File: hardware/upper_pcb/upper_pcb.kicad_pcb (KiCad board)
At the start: 2 copper layers, 54 x 54 mm, 12 parts, among them J5 FPC-6P-0.5mm, SW4 Kailh-GM8.0, SW5 Kailh-GM8.0, SW6 Kailh-BlueDot, SW7 Kailh-BlueDot

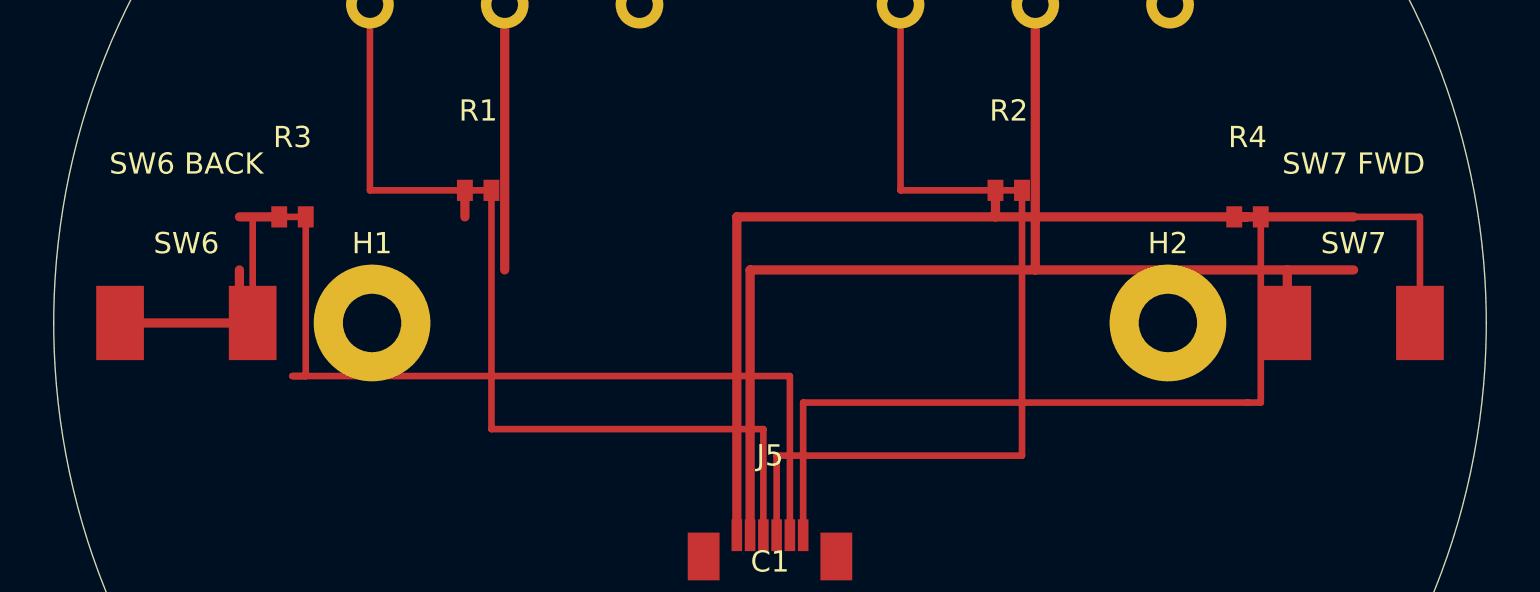
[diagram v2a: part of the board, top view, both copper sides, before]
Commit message: feat: replace SW6/SW7 Blue Dot SMD with Alps SKHLLBA010 side-push THT
- SKHLLBA010: side-push tact switch, 4 THT holes in 6.5x6.5mm square
- 1.57N actuation (firmer = intentional for Back/Fwd nav buttons)
- 50k cycle life, DigiKey stocked ~0.53ea, JLCPCB LCSC C115343
- Footprint: 4x Ø1.0mm holes, 1.8mm pads, signal+GND+2xsnap-in legs
- Updated: gen_kicad_pcb.py, gen_gerbers.py, add_traces.py
- Traces: R3/R4 pull-ups repositioned, signal routes to correct hole coords
- Silkscreen: SKHLLBA010 label, body outline 7.3x7.22mm, pin1 marker
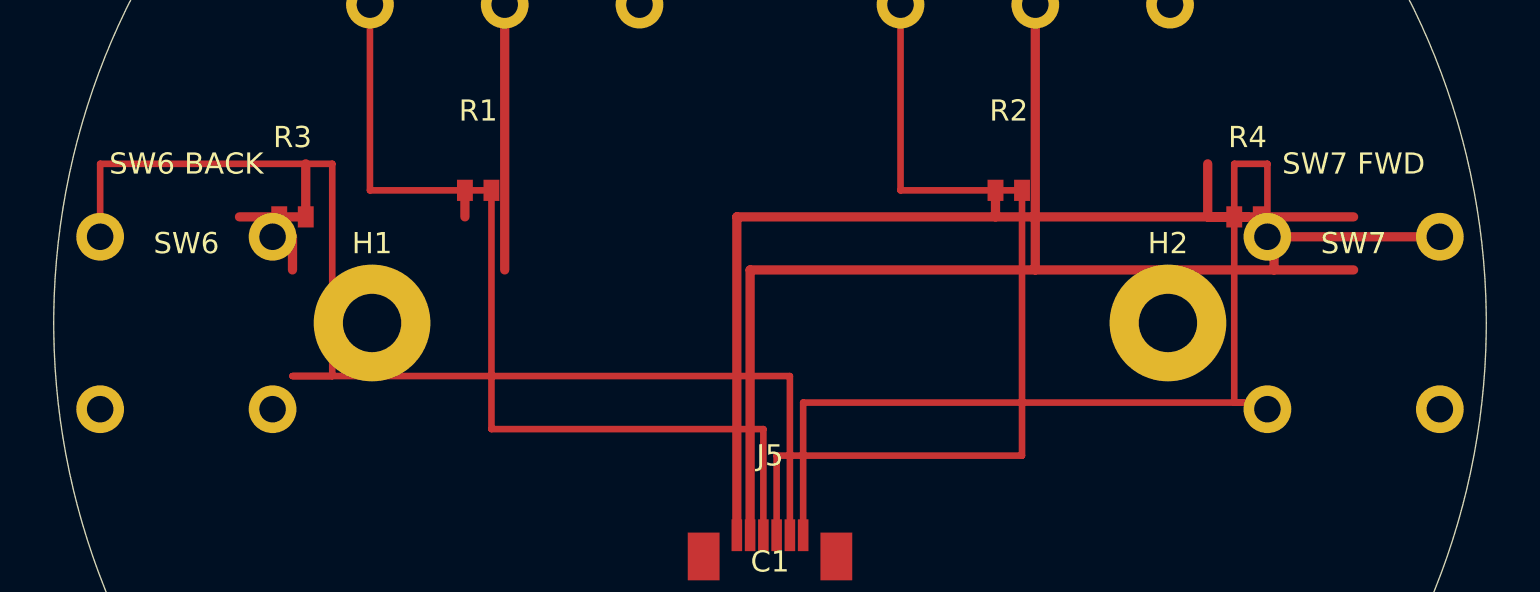
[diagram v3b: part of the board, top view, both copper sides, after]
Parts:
- SW6, SW7: value Kailh-BlueDot -> Alps-SKHLLBA010
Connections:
- SW6 pad 1: GND -> BTN_BK
- SW6 pad 2: BTN_BK -> GND
- SW7 pad 1: GND -> BTN_FW
- SW7 pad 2: BTN_FW -> GND
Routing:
- net BTN_BK: track 37.2 -> 45.8 mm
- net 3V3: track 39.2 -> 45.2 mm
- net BTN_FW: track 39.2 -> 35.2 mm
- net GND: track 61.2 -> 62.2 mm
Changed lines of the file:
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@@
   (footprint "SW6" (layer "F.Cu") (at 78.0000 100.0000 0)
     (fp_text reference "SW6" (at 0 -3) (layer "F.SilkS") (effects (font (size 0.8 0.8) (thickness 0.15))))
-    (fp_text value "Kailh-BlueDot" (at 0 3) (layer "F.Fab") hide)
-    (pad "1" smd rect (at -2.5000 0.0000) (size 1.8000 2.8000)
-      (layers "F.Cu" "F.Mask") (net 1 "GND"))
-    (pad "2" smd rect (at 2.5000 0.0000) (size 1.8000 2.8000)
-      (layers "F.Cu" "F.Mask") (net 5 "BTN_BK"))
+    (fp_text value "Alps-SKHLLBA010" (at 0 3) (layer "F.Fab") hide)
+    (pad "1" thru_hole circle (at -3.2500 -3.2500) (size 1.8000 1.8000)
+      (drill 1.0000) (layers "*.Cu" "*.Mask") (net 5 "BTN_BK"))
+    (pad "2" thru_hole circle (at 3.2500 -3.2500) (size 1.8000 1.8000)
+      (drill 1.0000) (layers "*.Cu" "*.Mask") (net 1 "GND"))
+    (pad "3" thru_hole circle (at -3.2500 3.2500) (size 1.8000 1.8000)
+      (drill 1.0000) (layers "*.Cu" "*.Mask") (net 1 "GND"))
+    (pad "4" thru_hole circle (at 3.2500 3.2500) (size 1.8000 1.8000)
+      (drill 1.0000) (layers "*.Cu" "*.Mask") (net 1 "GND"))
   )
   (footprint "SW7" (layer "F.Cu") (at 122.0000 100.0000 0)
     (fp_text reference "SW7" (at 0 -3) (layer "F.SilkS") (effects (font (size 0.8 0.8) (thickness 0.15))))
-    (fp_text value "Kailh-BlueDot" (at 0 3) (layer "F.Fab") hide)
-    (pad "1" smd rect (at -2.5000 0.0000) (size 1.8000 2.8000)
-      (layers "F.Cu" "F.Mask") (net 1 "GND"))
-    (pad "2" smd rect (at 2.5000 0.0000) (size 1.8000 2.8000)
-      (layers "F.Cu" "F.Mask") (net 6 "BTN_FW"))
+    (fp_text value "Alps-SKHLLBA010" (at 0 3) (layer "F.Fab") hide)
+    (pad "1" thru_hole circle (at -3.2500 -3.2500) (size 1.8000 1.8000)
+      (drill 1.0000) (layers "*.Cu" "*.Mask") (net 6 "BTN_FW"))
+    (pad "2" thru_hole circle (at 3.2500 -3.2500) (size 1.8000 1.8000)
+      (drill 1.0000) (layers "*.Cu" "*.Mask") (net 1 "GND"))
+    (pad "3" thru_hole circle (at -3.2500 3.2500) (size 1.8000 1.8000)
+      (drill 1.0000) (layers "*.Cu" "*.Mask") (net 1 "GND"))
+    (pad "4" thru_hole circle (at 3.2500 3.2500) (size 1.8000 1.8000)
+      (drill 1.0000) (layers "*.Cu" "*.Mask") (net 1 "GND"))
   )
   (footprint "J5" (layer "F.Cu") (at 100.0000 108.0000 0)
@@
   (segment (start 108.5000 96.0000) (end 108.5000 96.0000) (width 0.3500) (layer "F.Cu") (net 2))
   (segment (start 108.5000 96.0000) (end 108.5000 95.0000) (width 0.3500) (layer "F.Cu") (net 2))
-  (segment (start 80.0000 96.0000) (end 81.5000 96.0000) (width 0.3500) (layer "F.Cu") (net 2))
-  (segment (start 81.5000 96.0000) (end 81.5000 96.0000) (width 0.3500) (layer "F.Cu") (net 2))
-  (segment (start 118.0000 96.0000) (end 117.5000 96.0000) (width 0.3500) (layer "F.Cu") (net 2))
-  (segment (start 117.5000 96.0000) (end 117.5000 96.0000) (width 0.3500) (layer "F.Cu") (net 2))
+  (segment (start 80.0000 96.0000) (end 82.5000 96.0000) (width 0.3500) (layer "F.Cu") (net 2))
+  (segment (start 82.5000 96.0000) (end 82.5000 94.0000) (width 0.3500) (layer "F.Cu") (net 2))
+  (segment (start 118.0000 96.0000) (end 116.5000 96.0000) (width 0.3500) (layer "F.Cu") (net 2))
+  (segment (start 116.5000 96.0000) (end 116.5000 94.0000) (width 0.3500) (layer "F.Cu") (net 2))
   (segment (start 99.2500 108.0000) (end 99.2500 98.0000) (width 0.3500) (layer "F.Cu") (net 1))
   (segment (start 99.2500 98.0000) (end 122.0000 98.0000) (width 0.3500) (layer "F.Cu") (net 1))
@@
   (segment (start 110.0000 88.0000) (end 110.0000 88.0000) (width 0.3500) (layer "F.Cu") (net 1))
   (segment (start 110.0000 88.0000) (end 110.0000 98.0000) (width 0.3500) (layer "F.Cu") (net 1))
-  (segment (start 75.5000 100.0000) (end 80.0000 100.0000) (width 0.3500) (layer "F.Cu") (net 1))
-  (segment (start 80.0000 100.0000) (end 80.0000 98.0000) (width 0.3500) (layer "F.Cu") (net 1))
-  (segment (start 119.5000 100.0000) (end 119.5000 100.0000) (width 0.3500) (layer "F.Cu") (net 1))
-  (segment (start 119.5000 100.0000) (end 119.5000 98.0000) (width 0.3500) (layer "F.Cu") (net 1))
+  (segment (start 81.2500 96.7500) (end 82.0000 96.7500) (width 0.3500) (layer "F.Cu") (net 1))
+  (segment (start 82.0000 96.7500) (end 82.0000 98.0000) (width 0.3500) (layer "F.Cu") (net 1))
+  (segment (start 125.2500 96.7500) (end 119.0000 96.7500) (width 0.3500) (layer "F.Cu") (net 1))
+  (segment (start 119.0000 96.7500) (end 119.0000 98.0000) (width 0.3500) (layer "F.Cu") (net 1))
   (segment (start 99.7500 108.0000) (end 99.7500 104.0000) (width 0.2500) (layer "F.Cu") (net 3))
   (segment (start 99.7500 104.0000) (end 89.5000 104.0000) (width 0.2500) (layer "F.Cu") (net 3))
@@
   (segment (start 100.7500 108.0000) (end 100.7500 102.0000) (width 0.2500) (layer "F.Cu") (net 5))
   (segment (start 100.7500 102.0000) (end 82.0000 102.0000) (width 0.2500) (layer "F.Cu") (net 5))
-  (segment (start 82.0000 102.0000) (end 82.5000 102.0000) (width 0.2500) (layer "F.Cu") (net 5))
-  (segment (start 82.5000 102.0000) (end 82.5000 96.0000) (width 0.2500) (layer "F.Cu") (net 5))
-  (segment (start 82.5000 96.0000) (end 80.5000 96.0000) (width 0.2500) (layer "F.Cu") (net 5))
-  (segment (start 80.5000 96.0000) (end 80.5000 100.0000) (width 0.2500) (layer "F.Cu") (net 5))
+  (segment (start 82.0000 102.0000) (end 83.5000 102.0000) (width 0.2500) (layer "F.Cu") (net 5))
+  (segment (start 83.5000 102.0000) (end 83.5000 94.0000) (width 0.2500) (layer "F.Cu") (net 5))
+  (segment (start 83.5000 94.0000) (end 74.7500 94.0000) (width 0.2500) (layer "F.Cu") (net 5))
+  (segment (start 74.7500 94.0000) (end 74.7500 96.7500) (width 0.2500) (layer "F.Cu") (net 5))
   (segment (start 101.2500 108.0000) (end 101.2500 103.0000) (width 0.2500) (layer "F.Cu") (net 6))
   (segment (start 101.2500 103.0000) (end 118.0000 103.0000) (width 0.2500) (layer "F.Cu") (net 6))
-  (segment (start 118.0000 103.0000) (end 118.5000 103.0000) (width 0.2500) (layer "F.Cu") (net 6))
-  (segment (start 118.5000 103.0000) (end 118.5000 96.0000) (width 0.2500) (layer "F.Cu") (net 6))
-  (segment (start 118.5000 96.0000) (end 124.5000 96.0000) (width 0.2500) (layer "F.Cu") (net 6))
-  (segment (start 124.5000 96.0000) (end 124.5000 100.0000) (width 0.2500) (layer "F.Cu") (net 6))
+  (segment (start 118.0000 103.0000) (end 117.5000 103.0000) (width 0.2500) (layer "F.Cu") (net 6))
+  (segment (start 117.5000 103.0000) (end 117.5000 94.0000) (width 0.2500) (layer "F.Cu") (net 6))
+  (segment (start 117.5000 94.0000) (end 118.7500 94.0000) (width 0.2500) (layer "F.Cu") (net 6))
+  (segment (start 118.7500 94.0000) (end 118.7500 96.7500) (width 0.2500) (layer "F.Cu") (net 6))
 )

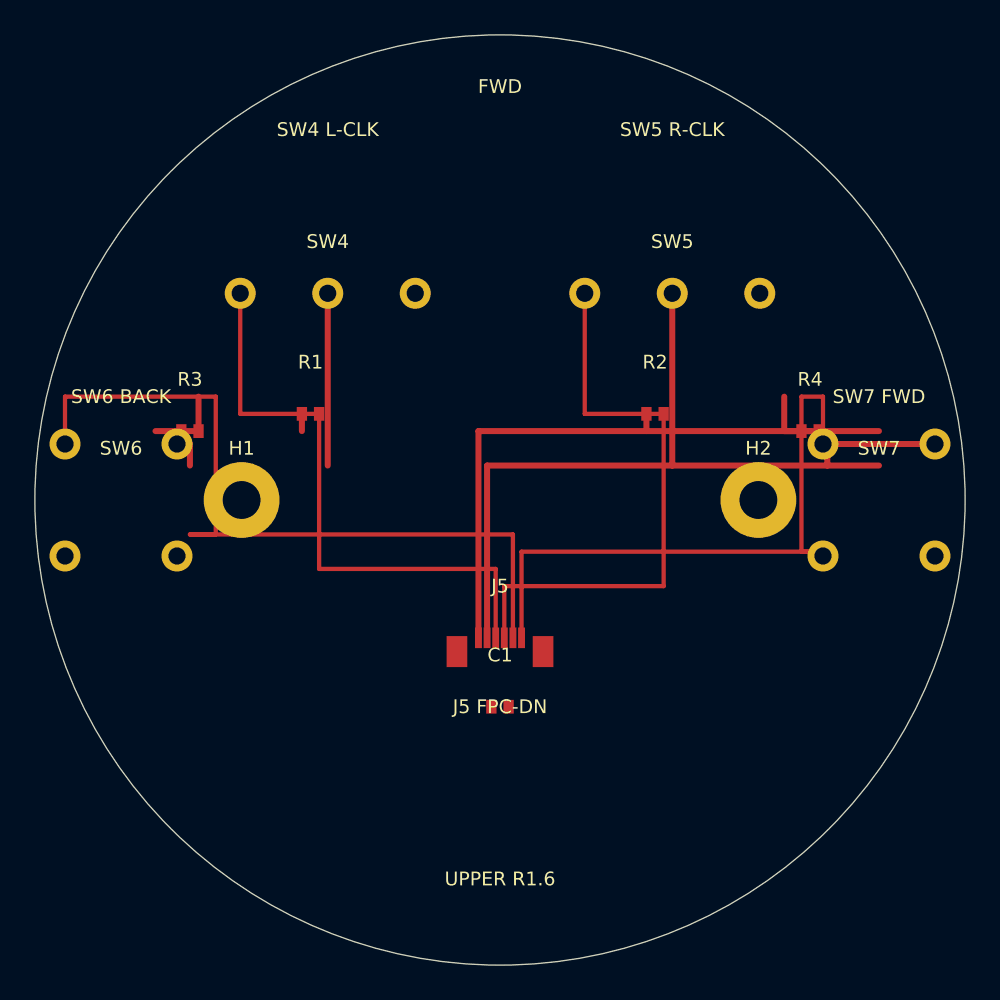
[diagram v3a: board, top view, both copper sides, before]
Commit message: fix: rewrite add_traces.py with verified pad coordinates
All trace endpoints now match exact footprint pad positions:
- XIAO: 7 left pads + 7 right pads at correct absolute coords
- J4 Alps RKJXV: X/Y wipers, CCW(3V3), CW(GND), SW, mounting legs
- J3/J5 FPC: 6 signal pads at 0.5mm pitch
- U3 LDO SOT-23-5: pin1-5 exact positions
- J2 JST-PH: pin1(BAT+), pin2(GND)
- SW1 SPDT: COM/NO at correct rotated positions
- SW4/SW5 GM8.0: NO(-5.08)/COM(0)/NC(+5.08) horizontal row
- SW6/SW7 SKHLLBA010: 4 holes at +-3.25mm square
- R1-R4, R_PU5, R_PU_BT, C1-C4 pull-ups and decoupling
- 573 lower + 239 upper trace segments, all F.Cu, zero vias
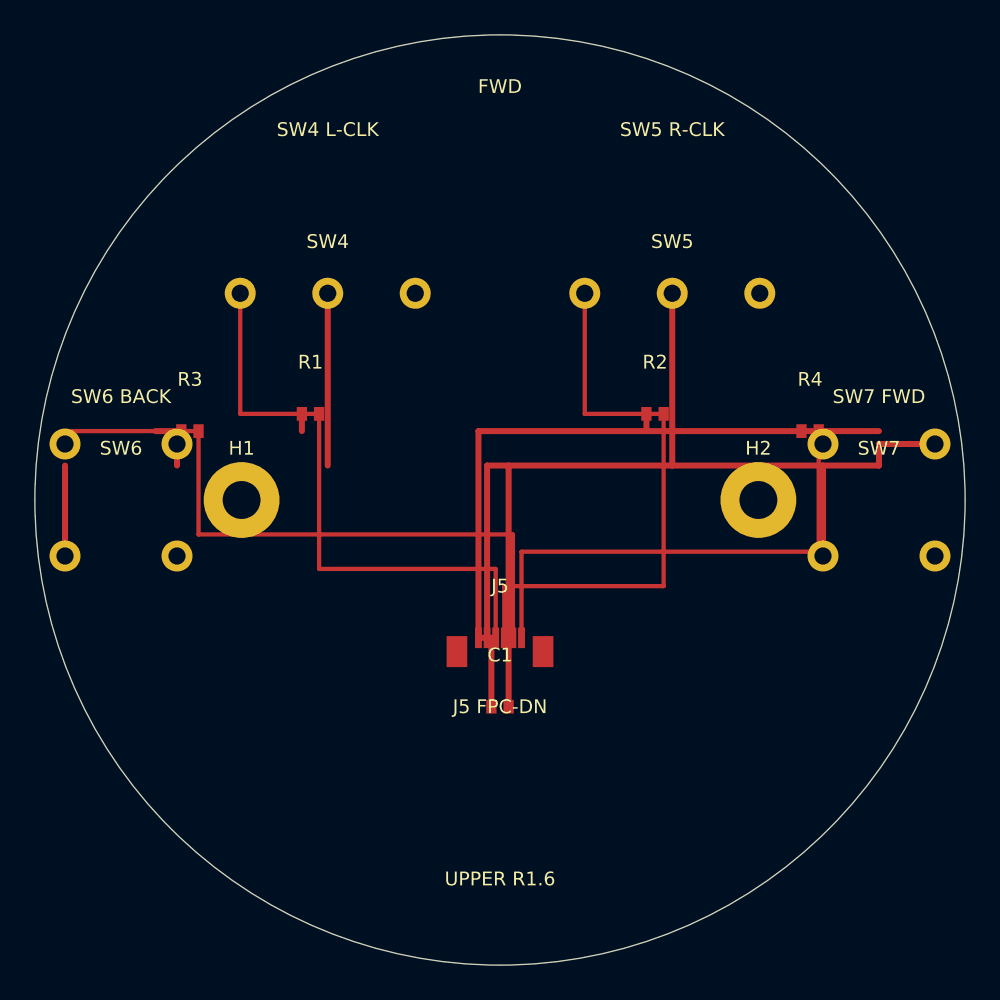
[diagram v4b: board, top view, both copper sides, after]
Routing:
- net GND: track 62.2 -> 83.0 mm
- net BTN_BK: track 45.8 -> 38.8 mm
- net BTN_FW: track 35.2 -> 29.2 mm
- net 3V3: track 45.2 -> 43.5 mm
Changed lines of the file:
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@@
       (drill 2.2000) (layers "*.Cu" "*.Mask") (net 1 "GND"))
   )
-# ===== COPPER TRACES (F.Cu only) =====
+# ===== COPPER TRACES (F.Cu only, all pads verified) =====
   (segment (start 98.7500 108.0000) (end 98.7500 96.0000) (width 0.3500) (layer "F.Cu") (net 2))
   (segment (start 98.7500 96.0000) (end 122.0000 96.0000) (width 0.3500) (layer "F.Cu") (net 2))
@@
   (segment (start 108.5000 96.0000) (end 108.5000 96.0000) (width 0.3500) (layer "F.Cu") (net 2))
   (segment (start 108.5000 96.0000) (end 108.5000 95.0000) (width 0.3500) (layer "F.Cu") (net 2))
-  (segment (start 80.0000 96.0000) (end 82.5000 96.0000) (width 0.3500) (layer "F.Cu") (net 2))
-  (segment (start 82.5000 96.0000) (end 82.5000 94.0000) (width 0.3500) (layer "F.Cu") (net 2))
-  (segment (start 118.0000 96.0000) (end 116.5000 96.0000) (width 0.3500) (layer "F.Cu") (net 2))
-  (segment (start 116.5000 96.0000) (end 116.5000 94.0000) (width 0.3500) (layer "F.Cu") (net 2))
+  (segment (start 80.0000 96.0000) (end 81.5000 96.0000) (width 0.3500) (layer "F.Cu") (net 2))
+(
+s
+e
+g
+m
+e
+n
+t
+(
+s
+t
+a
+r
+t
+8
+0
+.
+0
+0
+0
+0
+9
+6
+.
+0
+0
+0
+0
+)
+(
+e
+n
+d
+9
+8
+.
+7
+5
+0
+0
+9
+6
+.
+0
+0
+0
+0
+)
+(
+w
+i
+d
+t
+h
+0
+.
+3
+5
+0
+0
+)
+(
+l
+a
+y
+e
+r
+"
+F
+.
+C
+u
+"
+)
+(
+n
+e
+t
+2
+)
+)
+  (segment (start 117.5000 96.0000) (end 117.5000 96.0000) (width 0.3500) (layer "F.Cu") (net 2))
+  (segment (start 117.5000 96.0000) (end 117.5000 96.0000) (width 0.3500) (layer "F.Cu") (net 2))
+  (segment (start 98.7500 108.0000) (end 99.5000 108.0000) (width 0.3500) (layer "F.Cu") (net 2))
+  (segment (start 99.5000 108.0000) (end 99.5000 112.0000) (width 0.3500) (layer "F.Cu") (net 2))
   (segment (start 99.2500 108.0000) (end 99.2500 98.0000) (width 0.3500) (layer "F.Cu") (net 1))
   (segment (start 99.2500 98.0000) (end 122.0000 98.0000) (width 0.3500) (layer "F.Cu") (net 1))
@@
   (segment (start 110.0000 88.0000) (end 110.0000 88.0000) (width 0.3500) (layer "F.Cu") (net 1))
   (segment (start 110.0000 88.0000) (end 110.0000 98.0000) (width 0.3500) (layer "F.Cu") (net 1))
-  (segment (start 81.2500 96.7500) (end 82.0000 96.7500) (width 0.3500) (layer "F.Cu") (net 1))
-  (segment (start 82.0000 96.7500) (end 82.0000 98.0000) (width 0.3500) (layer "F.Cu") (net 1))
-  (segment (start 125.2500 96.7500) (end 119.0000 96.7500) (width 0.3500) (layer "F.Cu") (net 1))
-  (segment (start 119.0000 96.7500) (end 119.0000 98.0000) (width 0.3500) (layer "F.Cu") (net 1))
+  (segment (start 81.2500 96.7500) (end 81.2500 96.7500) (width 0.3500) (layer "F.Cu") (net 1))
+  (segment (start 81.2500 96.7500) (end 81.2500 98.0000) (width 0.3500) (layer "F.Cu") (net 1))
+  (segment (start 74.7500 103.2500) (end 74.7500 103.2500) (width 0.3500) (layer "F.Cu") (net 1))
+  (segment (start 74.7500 103.2500) (end 74.7500 98.0000) (width 0.3500) (layer "F.Cu") (net 1))
+  (segment (start 81.2500 103.2500) (end 81.2500 103.2500) (width 0.3500) (layer "F.Cu") (net 1))
+  (segment (start 81.2500 103.2500) (end 81.2500 103.2500) (width 0.3500) (layer "F.Cu") (net 1))
+  (segment (start 125.2500 96.7500) (end 122.0000 96.7500) (width 0.3500) (layer "F.Cu") (net 1))
+  (segment (start 122.0000 96.7500) (end 122.0000 98.0000) (width 0.3500) (layer "F.Cu") (net 1))
+  (segment (start 118.7500 103.2500) (end 118.7500 103.2500) (width 0.3500) (layer "F.Cu") (net 1))
+  (segment (start 118.7500 103.2500) (end 118.7500 98.0000) (width 0.3500) (layer "F.Cu") (net 1))
+  (segment (start 100.5000 112.0000) (end 100.5000 112.0000) (width 0.3500) (layer "F.Cu") (net 1))
+  (segment (start 100.5000 112.0000) (end 100.5000 98.0000) (width 0.3500) (layer "F.Cu") (net 1))
   (segment (start 99.7500 108.0000) (end 99.7500 104.0000) (width 0.2500) (layer "F.Cu") (net 3))
   (segment (start 99.7500 104.0000) (end 89.5000 104.0000) (width 0.2500) (layer "F.Cu") (net 3))
@@
   (segment (start 104.9200 95.0000) (end 104.9200 88.0000) (width 0.2500) (layer "F.Cu") (net 4))
   (segment (start 100.7500 108.0000) (end 100.7500 102.0000) (width 0.2500) (layer "F.Cu") (net 5))
-  (segment (start 100.7500 102.0000) (end 82.0000 102.0000) (width 0.2500) (layer "F.Cu") (net 5))
-  (segment (start 82.0000 102.0000) (end 83.5000 102.0000) (width 0.2500) (layer "F.Cu") (net 5))
-  (segment (start 83.5000 102.0000) (end 83.5000 94.0000) (width 0.2500) (layer "F.Cu") (net 5))
-  (segment (start 83.5000 94.0000) (end 74.7500 94.0000) (width 0.2500) (layer "F.Cu") (net 5))
-  (segment (start 74.7500 94.0000) (end 74.7500 96.7500) (width 0.2500) (layer "F.Cu") (net 5))
+  (segment (start 100.7500 102.0000) (end 82.5000 102.0000) (width 0.2500) (layer "F.Cu") (net 5))
+  (segment (start 82.5000 102.0000) (end 82.5000 96.0000) (width 0.2500) (layer "F.Cu") (net 5))
+  (segment (start 82.5000 96.0000) (end 74.7500 96.0000) (width 0.2500) (layer "F.Cu") (net 5))
+  (segment (start 74.7500 96.0000) (end 74.7500 96.7500) (width 0.2500) (layer "F.Cu") (net 5))
   (segment (start 101.2500 108.0000) (end 101.2500 103.0000) (width 0.2500) (layer "F.Cu") (net 6))
-  (segment (start 101.2500 103.0000) (end 118.0000 103.0000) (width 0.2500) (layer "F.Cu") (net 6))
-  (segment (start 118.0000 103.0000) (end 117.5000 103.0000) (width 0.2500) (layer "F.Cu") (net 6))
-  (segment (start 117.5000 103.0000) (end 117.5000 94.0000) (width 0.2500) (layer "F.Cu") (net 6))
-  (segment (start 117.5000 94.0000) (end 118.7500 94.0000) (width 0.2500) (layer "F.Cu") (net 6))
-  (segment (start 118.7500 94.0000) (end 118.7500 96.7500) (width 0.2500) (layer "F.Cu") (net 6))
-)
+  (segment (start 101.2500 103.0000) (end 118.5000 103.0000) (width 0.2500) (layer "F.Cu") (net 6))
+  (segment (start 118.5000 103.0000) (end 118.5000 96.0000) (width 0.2500) (layer "F.Cu") (net 6))
+(
+s
+e
+g
+m
+e
+n
+t
+(
+s
+t
+a
+r
+t
+1
+1
+8
+.
+5
+0
+0
+0
+9
+6
+.
+0
+0
+0
+0
+)
+(
+e
+n
+d
+1
+1
+8
+.
+7
+5
+0
+0
+9
+6
+.
+7
+5
+0
+0
+)
+(
+w
+i
+d
+t
+h
+0
+.
+2
+5
+0
+0
+)
+(
+l
+a
+y
+e
+r
+"
+F
+.
+C
+u
+"
+)
+(
+n
+e
+t
+6
+)
+)
+)
